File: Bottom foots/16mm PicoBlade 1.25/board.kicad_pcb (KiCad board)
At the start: 2 copper layers, 24 x 33.2 mm, 17 parts, among them J1 Conn_01x06, J10 Conn_01x01, J11 Conn_01x03, J12 Conn_01x01, J13 Conn_01x01, J2 Conn_01x03, J3 Conn_01x03, J4 Conn_01x03, J5 Conn_01x03, J6 Conn_01x01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

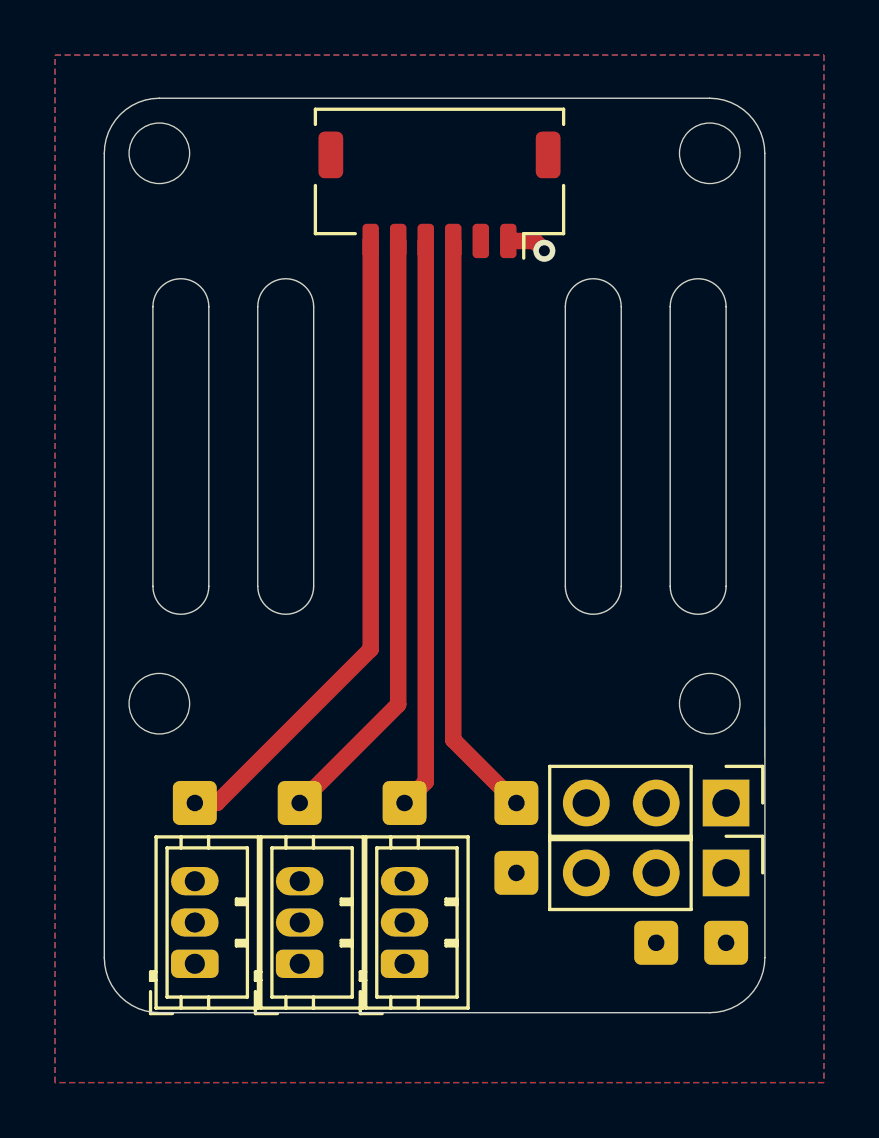
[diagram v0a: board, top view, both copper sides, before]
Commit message: Bottom foots.
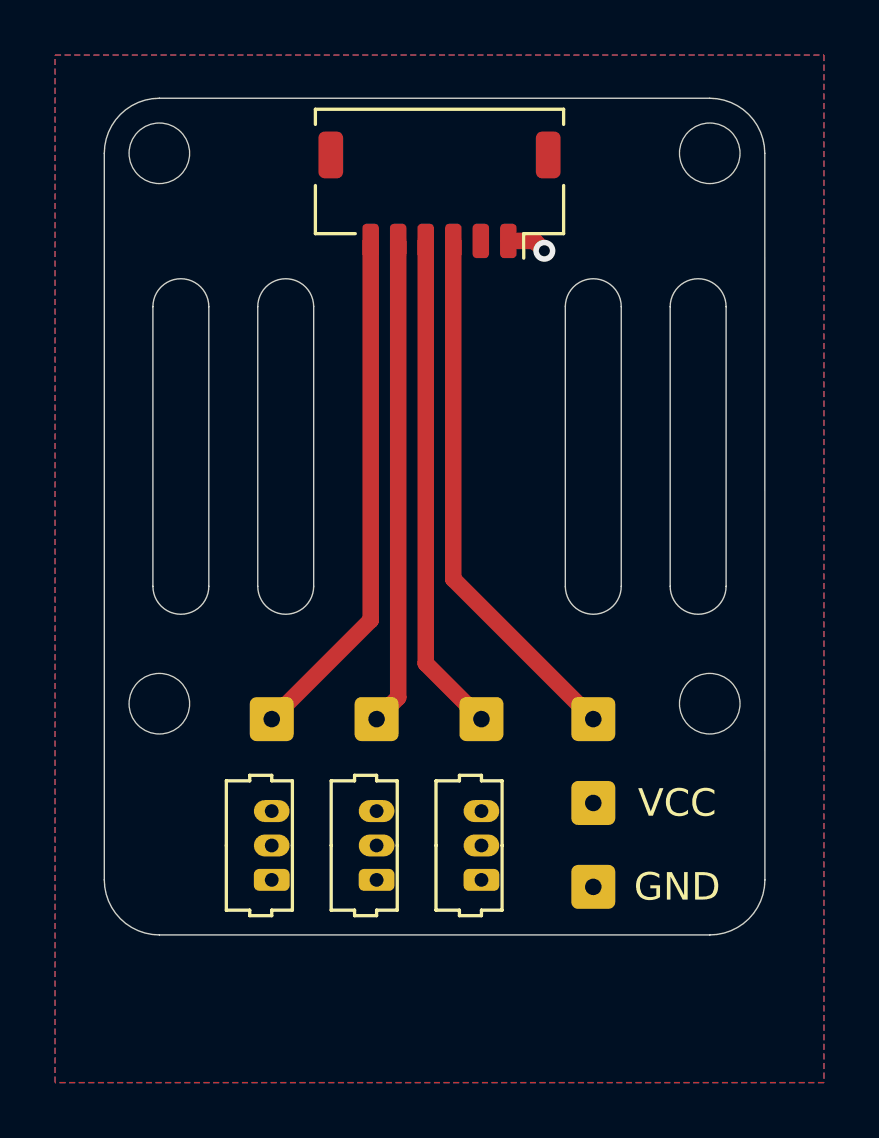
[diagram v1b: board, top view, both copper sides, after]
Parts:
- removed J11, J5: Conn_01x03, Connector_PinHeader_2.54mm:PinHeader_1x03_P2.54mm_Vertical
- removed J12: Conn_01x01, Connector_Wire:SolderWire-0.1sqmm_1x01_D0.4mm_OD1mm
- J2, J3, J4: footprint RC-PCBs:JST_ZH_B3B-ZR_1x03_P1.50mm_Vertical -> RC-PCBs:Molex_PicoBlade_53047-0310_1x03_P1.25mm_Vertical
- moved J10 5.57 mm to (118.4, 126.0)
- moved J6 5.24 mm to (118.4, 129.0)
- moved J2 4.13 mm to (106.7, 128.8)
- moved J3 4.13 mm to (110.5, 128.8)
- moved J4 4.13 mm to (114.3, 128.8)
- moved J13 4.13 mm to (106.7, 122.9)
- moved J9 4.13 mm to (118.4, 122.9)
- moved J7 4.13 mm to (110.5, 122.9)
- moved J8 4.13 mm to (114.3, 122.9)
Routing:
- net Net-(J1-Pad6): track 23.5 -> 18.9 mm
- net Net-(J1-Pad5): track 21.9 -> 17.7 mm
- net Net-(J1-Pad4): track 20.7 -> 18.2 mm
- net Net-(J1-Pad3): track 21.4 -> 19.5 mm
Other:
- board size 24 x 33.2 mm -> 24 x 30.4 mm
- board text added: "GND"
- board text added: "VCC"
